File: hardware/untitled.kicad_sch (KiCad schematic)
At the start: 4 parts, among them U2 H5TQ4G63EFR, U3 H5TQ4G63EFR

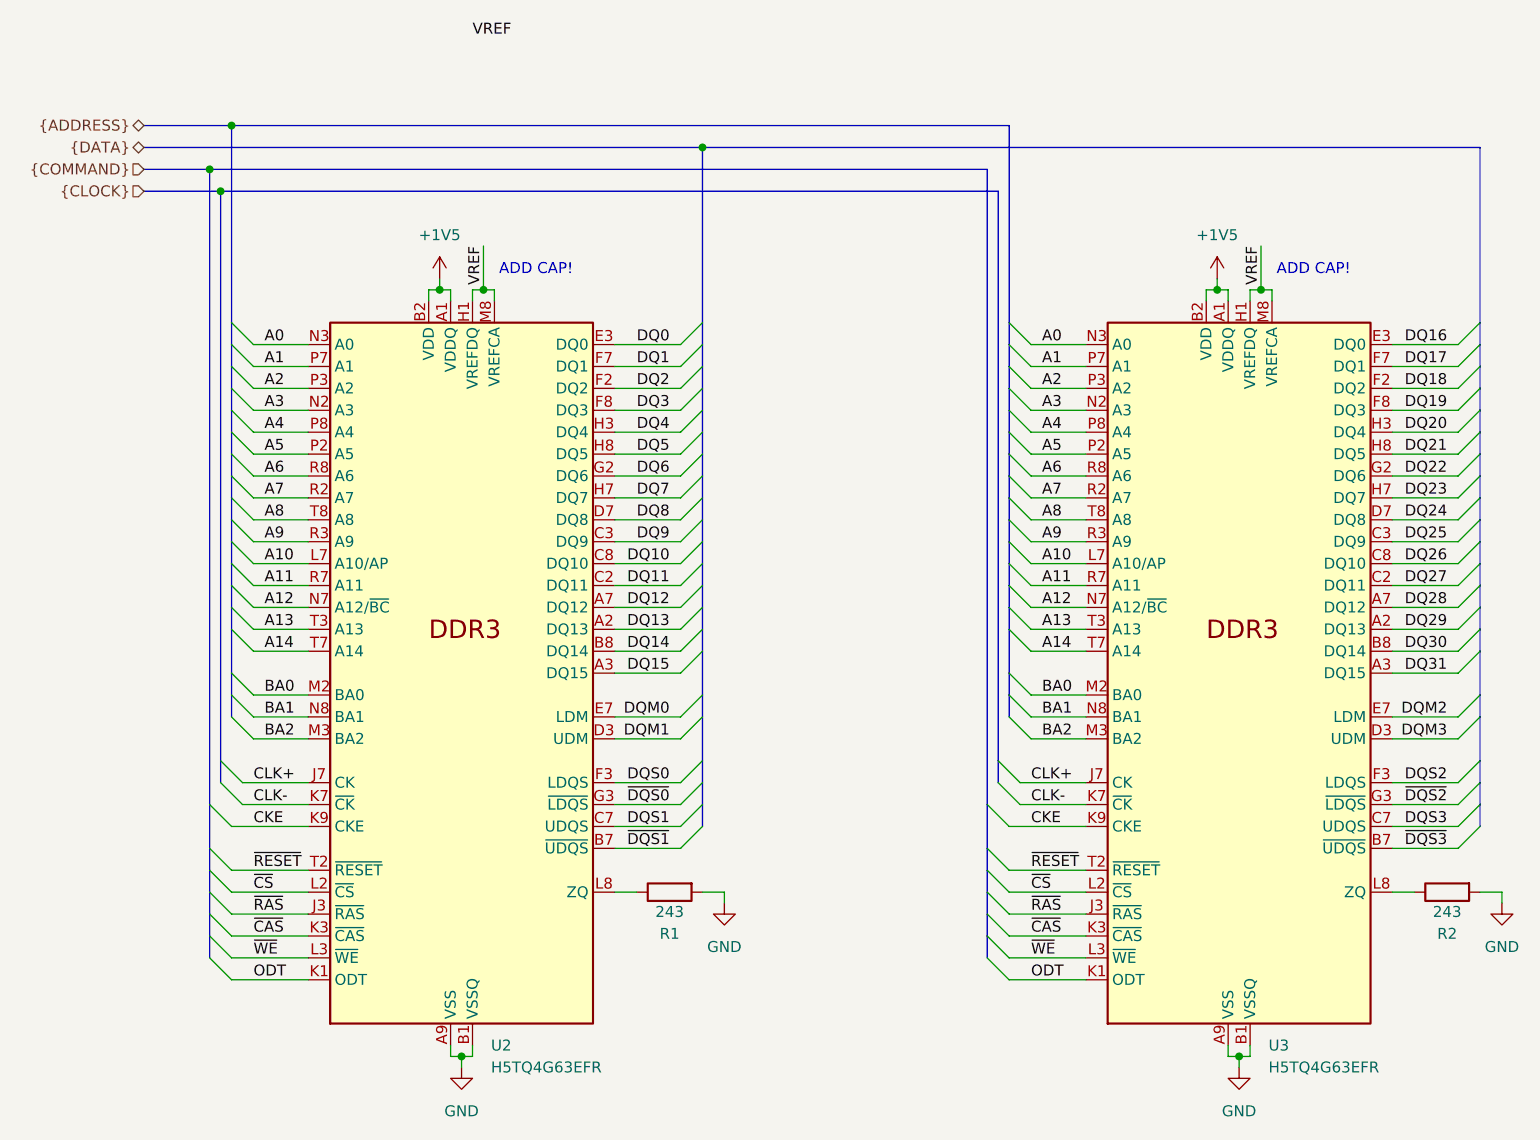
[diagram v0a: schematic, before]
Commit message: Routed DDR3
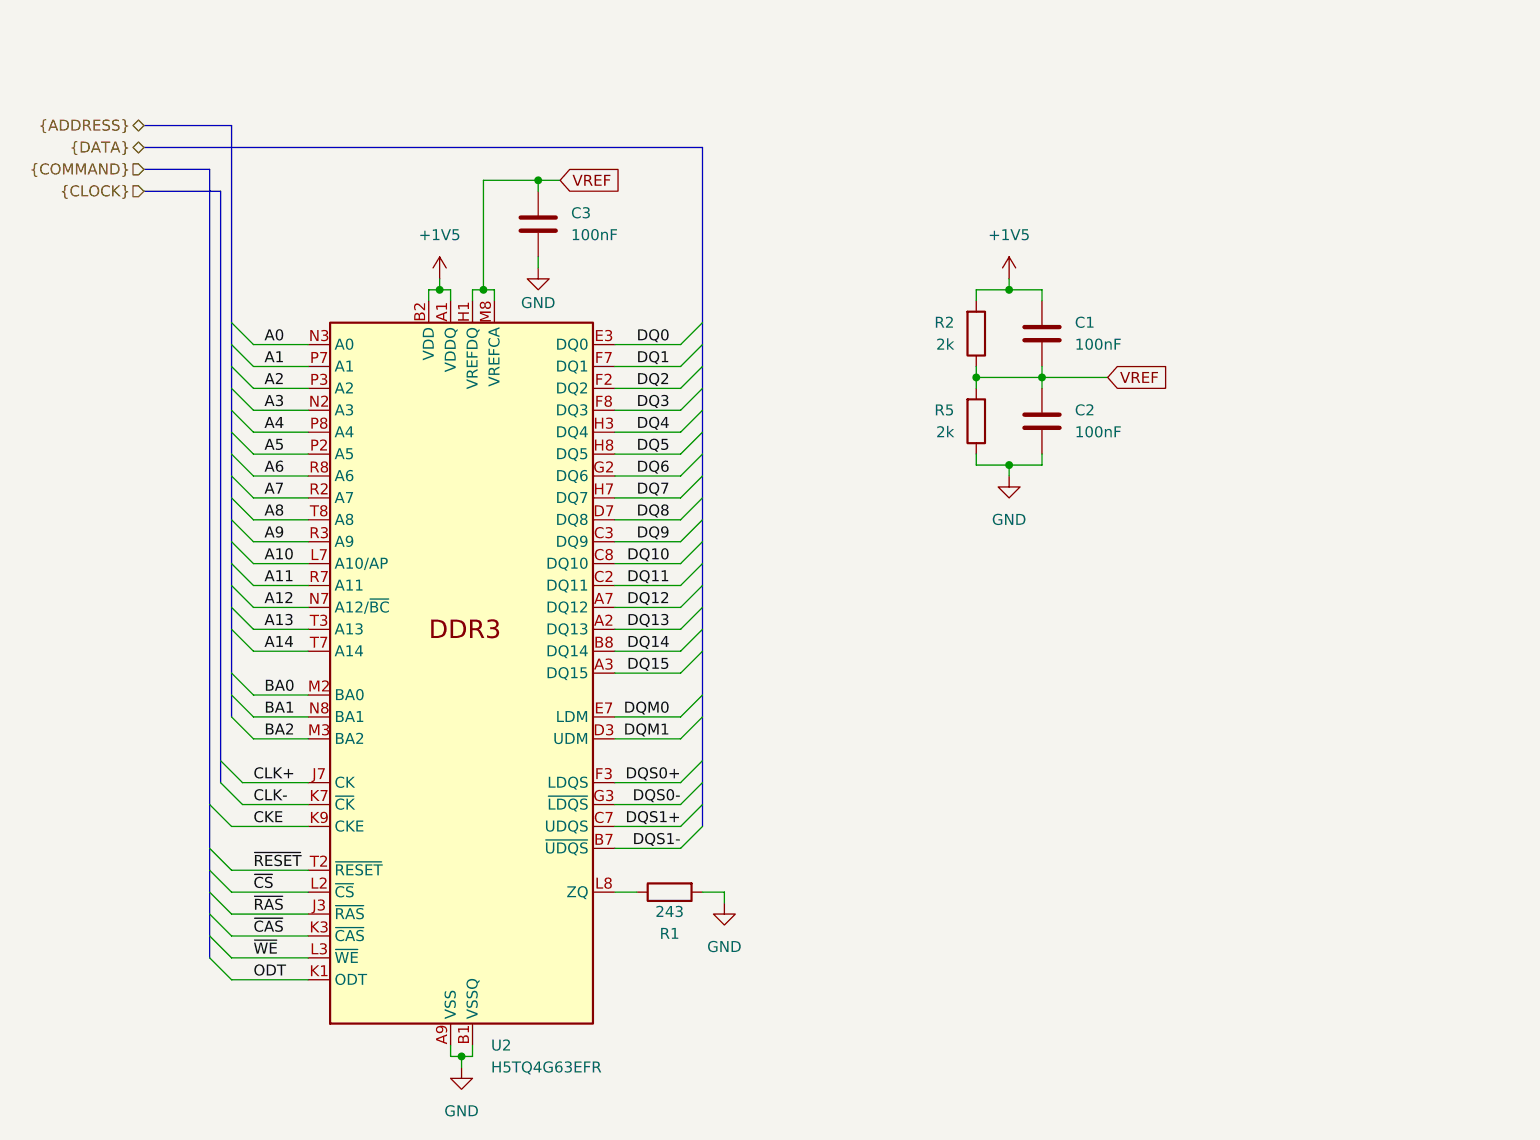
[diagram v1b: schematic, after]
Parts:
- removed U3: H5TQ4G63EFR, Package_BGA:FBGA-96_7.5x13mm_Layout9x16_P0.8mm, symbol cm0:H5TQ4G63EFR
- added C1, C2, C3: 100nF, Capacitor_SMD:C_0402_1005Metric, symbol Device:C
- added R5: 2k, Resistor_SMD:R_0603_1608Metric, symbol Device:R
- R1: footprint (none) -> Resistor_SMD:R_0603_1608Metric
- R2: value 243 -> 2k; footprint (none) -> Resistor_SMD:R_0603_1608Metric
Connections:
- net +1V5: now also R2.2, C1.1
- net GND: now also C2.2, C3.2, R5.1; no longer R2.2
- net VREF: now also R2.1, C1.2, C2.1, C3.1, R5.2
- net DQS0 renamed DQS0+
- net DQS1 renamed DQS1+
- net ~{DQS0} renamed DQS0-
- net ~{DQS1} renamed DQS1-
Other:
- note removed: "ADD CAP!"
